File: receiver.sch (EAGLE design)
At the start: 28 parts

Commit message: added buzzer.
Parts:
- added BUZZER: (no value), pinhead:PINHD-1X3/90
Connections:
- new net N$18: BUZZER.2, ESP-12E.GPIO16
- net GND: now also BUZZER.3
- net VCC: now also BUZZER.1
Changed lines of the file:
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@@
 <part name="SUPPLY6" library="supply2" library_urn="urn:adsk.eagle:library:372" deviceset="VCC" device="" value="+3V3"/>
 <part name="U$1" library="diy-modules" deviceset="BATTERY-CHARGER-LI-PROT" device=""/>
+<part name="BUZZER" library="pinhead" library_urn="urn:adsk.eagle:library:325" deviceset="PINHD-1X3" device="/90" package3d_urn="urn:adsk.eagle:package:22459/2"/>
+<part name="SUPPLY10" library="supply2" library_urn="urn:adsk.eagle:library:372" deviceset="VCC" device="" value="+3V3"/>
+<part name="GND13" library="supply1" library_urn="urn:adsk.eagle:library:371" deviceset="GND" device=""/>
 </parts>
 <sheets>
@@
 <instance part="SUPPLY6" gate="G$1" x="-27.94" y="58.42"/>
 <instance part="U$1" gate="G$1" x="-27.94" y="109.22"/>
+<instance part="BUZZER" gate="A" x="-12.7" y="71.12"/>
+<instance part="SUPPLY10" gate="G$1" x="-20.32" y="78.74"/>
+<instance part="GND13" gate="1" x="-20.32" y="63.5"/>
 </instances>
 <busses>
@@
 <wire x1="15.24" y1="116.84" x2="15.24" y2="119.38" width="0.1524" layer="91"/>
 </segment>
+<segment>
+<pinref part="BUZZER" gate="A" pin="1"/>
+<wire x1="-15.24" y1="73.66" x2="-20.32" y2="73.66" width="0.1524" layer="91"/>
+<wire x1="-20.32" y1="73.66" x2="-20.32" y2="76.2" width="0.1524" layer="91"/>
+<pinref part="SUPPLY10" gate="G$1" pin="VCC"/>
+</segment>
 </net>
 <net name="GND" class="0">
@@
 <wire x1="-10.16" y1="101.6" x2="-12.7" y2="101.6" width="0.1524" layer="91"/>
 </segment>
+<segment>
+<pinref part="BUZZER" gate="A" pin="3"/>
+<wire x1="-15.24" y1="68.58" x2="-20.32" y2="68.58" width="0.1524" layer="91"/>
+<pinref part="GND13" gate="1" pin="GND"/>
+<wire x1="-20.32" y1="68.58" x2="-20.32" y2="66.04" width="0.1524" layer="91"/>
+</segment>
 </net>
 <net name="N$1" class="0">
@@
 </segment>
 </net>
+<net name="N$18" class="0">
+<segment>
+<pinref part="ESP-12E" gate="G$1" pin="GPIO16"/>
+<wire x1="40.64" y1="66.04" x2="-7.62" y2="66.04" width="0.1524" layer="91"/>
+<wire x1="-7.62" y1="66.04" x2="-7.62" y2="83.82" width="0.1524" layer="91"/>
+<wire x1="-7.62" y1="83.82" x2="-25.4" y2="83.82" width="0.1524" layer="91"/>
+<wire x1="-25.4" y1="83.82" x2="-25.4" y2="71.12" width="0.1524" layer="91"/>
+<pinref part="BUZZER" gate="A" pin="2"/>
+<wire x1="-25.4" y1="71.12" x2="-15.24" y2="71.12" width="0.1524" layer="91"/>
+</segment>
+</net>

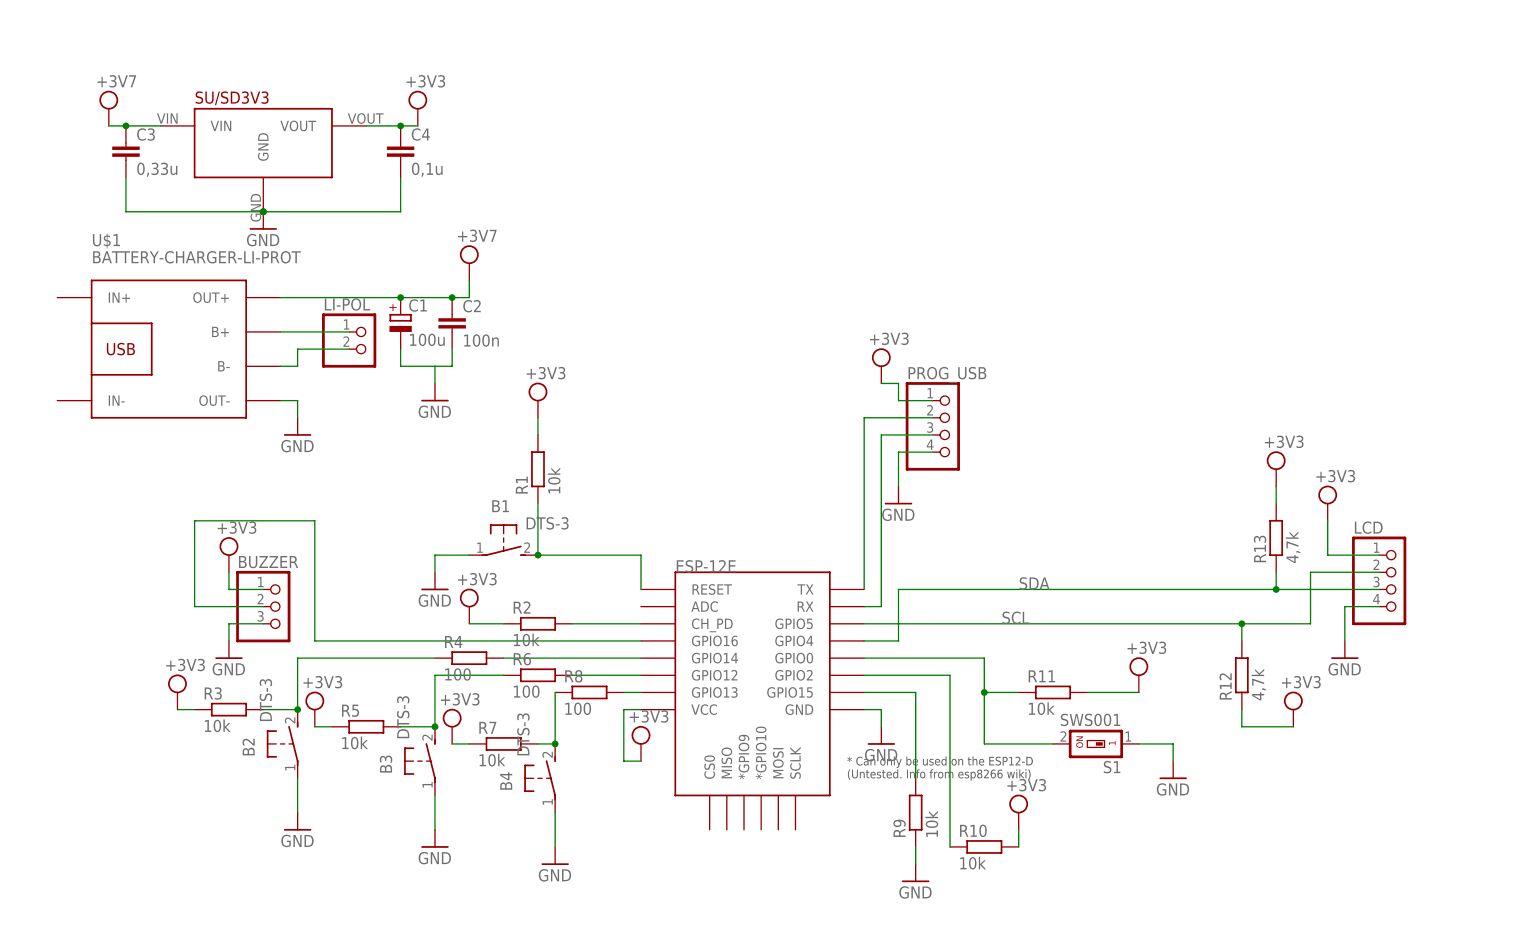
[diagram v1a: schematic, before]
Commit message: Added resisotr to busser input line.
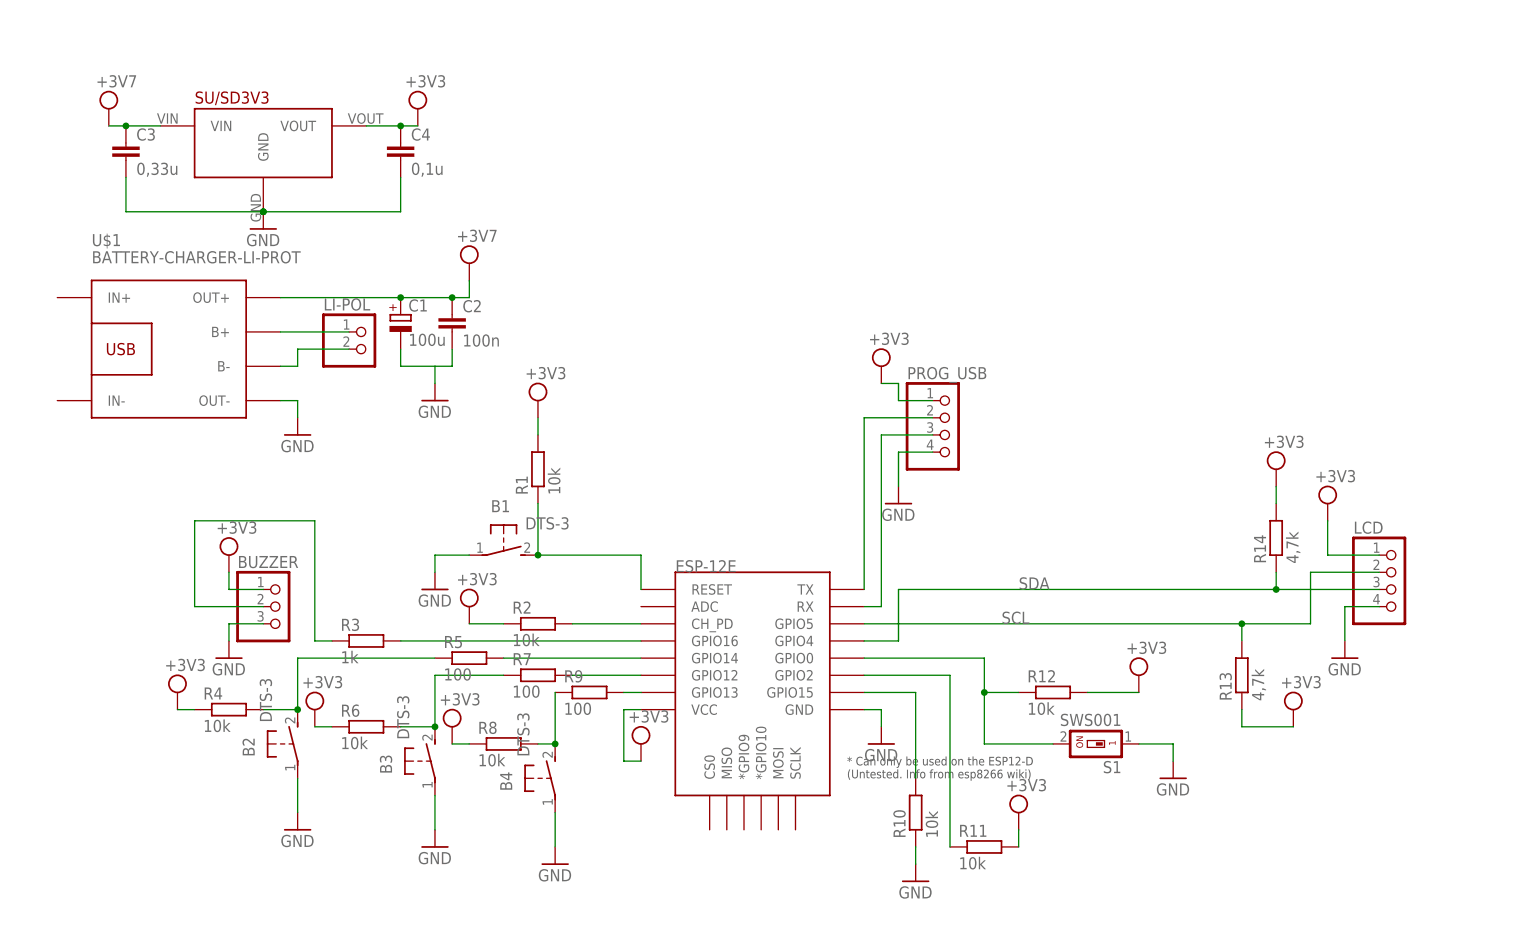
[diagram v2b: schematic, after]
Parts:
- added R14: 4,7k, rcl:R-EU_0204/5
- R12: value 4,7k -> 10k
- R3: value 10k -> 1k
- R4, R6, R8: value 100 -> 10k
- R5, R7, R9: value 10k -> 100
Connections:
- new net N$15: ESP-12E.GPIO16, R3.2
- net GND: now also R10.1; no longer R9.1
- net N$10: now also R9.2; no longer R8.2
- net N$11: now also R10.2; no longer R9.2
- net N$12: now also R5.2; no longer R4.2
- net N$13: now also R4.2, R5.1; no longer R3.2, R4.1
- net N$14: now also R6.2, R7.1; no longer R5.2, R6.1
- net N$18: now also R3.1; no longer ESP-12E.GPIO16
- net N$3: now also R12.1; no longer R11.1
- net N$4: now also R11.1; no longer R10.1
- net N$7: now also R7.2; no longer R6.2
- net N$8: now also R8.2, R9.1; no longer R7.2, R8.1
- net SCL: now also R13.2; no longer R12.2
- net SDA: now also R14.1; no longer R13.1
- net VCC: now also R12.2, R13.1, R14.2, R4.1, R6.1, R8.1; no longer R10.2, R12.1, R13.2, R3.1, R5.1, R7.1
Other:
- moved on the sheet: R10, R11, R12, R13, R3, R4, R5, R6, R7, R8, R9

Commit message: Changed some resistors from 10k for 2k2 and added resisors 100 to reset and gpio0 pin.
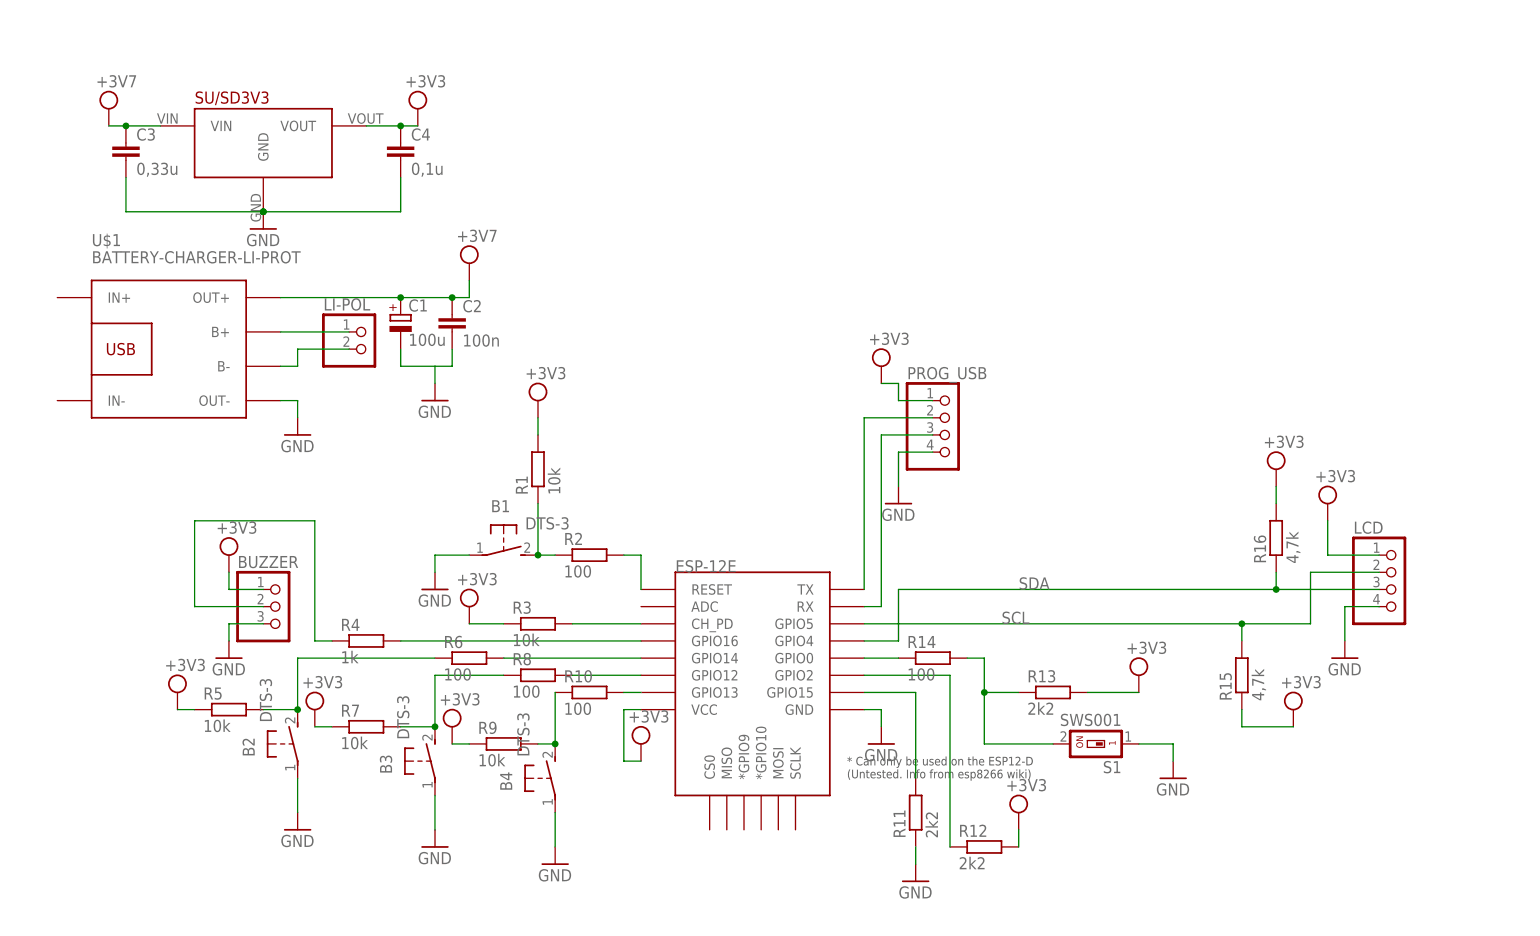
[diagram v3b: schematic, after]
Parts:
- added R15, R16: 4,7k, rcl:R-EU_0204/5
- R10, R2, R6, R8: value 10k -> 100
- R11, R12: value 10k -> 2k2
- R13: value 4,7k -> 2k2
- R14: value 4,7k -> 100
- R3: value 1k -> 10k
- R4: value 10k -> 1k
- R5, R7, R9: value 100 -> 10k
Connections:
- new net N$17: ESP-12E.RESET, R2.2
- new net N$19: ESP-12E.GPIO0, R14.1
- net GND: now also R11.1; no longer R10.1
- net N$1: now also R2.1; no longer ESP-12E.RESET
- net N$10: now also R10.2; no longer R9.2
- net N$11: now also R11.2; no longer R10.2
- net N$12: now also R6.2; no longer R5.2
- net N$13: now also R5.2, R6.1; no longer R4.2, R5.1
- net N$14: now also R7.2, R8.1; no longer R6.2, R7.1
- net N$15: now also R4.2; no longer R3.2
- net N$18: now also R4.1; no longer R3.1
- net N$2: now also R3.2; no longer R2.2
- net N$3: now also R13.1, R14.2; no longer ESP-12E.GPIO0, R12.1
- net N$4: now also R12.1; no longer R11.1
- net N$7: now also R8.2; no longer R7.2
- net N$8: now also R10.1, R9.2; no longer R8.2, R9.1
- net SCL: now also R15.2; no longer R13.2
- net SDA: now also R16.1; no longer R14.1
- net VCC: now also R13.2, R15.1, R16.2, R3.1, R5.1, R7.1, R9.1; no longer R11.2, R13.1, R14.2, R2.1, R4.1, R6.1, R8.1
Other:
- moved on the sheet: R10, R11, R12, R13, R14, R2, R3, R4, R5, R6, R7, R8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
